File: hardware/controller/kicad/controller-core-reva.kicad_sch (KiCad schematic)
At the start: 188 parts, among them J101 12V_ISOLATED_INPUT / JST XH, J102 STM_SWD / 1x6 2.54mm, J103 ESP_UART / 1x6 2.54mm, J104 UI_LINK / WR-MM 16, J105 JP13 NTC / 2 vías, J106 JP5 FLOW ADAPTER / VCC-GND-OC, J107 JP14 DOOR / contacto seco, J108 JP16 VISUAL V1..V8 / XH-8, J109 JP22 WATER / RED-WHITE-BLACK, J110 USB-C SERVICE / USB 2.0, J111 USB BENCH POWER / OPEN, J112 24V_ACTUATOR_INPUT / JST XH, J113 JP3 VALVE / A2506, J114 POWER MONITOR / MEASURE ONLY, J115 JP8 GRINDER / 320VDC, J116 JP19 HEATER / 1900W 27R5, J117 JP24 PUMP / 230VAC, J118 JP17 MAINS / L-N, J119 JP1 PE TO BOILER, J120 JP9 PE INPUT, J121 24V INTERNAL SELECT / OPEN FO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, K701 G5RL-1A-E-TV8 DC24, Q501 SI2308A, Q701 SI2308A / relay coil, Q703 BTA24-800BWRG / heater, Q704 BTA24-800BWRG / pump, Q705 SI2308A / heater opto LED, Q706 SI2308A / pump opto LED, Q707 SI2308A / grinder opto LED, Q708 BTA24-800BWRG / grinder, U101 STM32G431RBT6, U201 ESP32-S3-WROOM-1U-N8R8, U203 USBLC6-2SC6, U301 AP63203WU-7, U302 TPS22918DBVR, U303 AP63200WU-7 / 24V to 12V, U501 DRV8876PWPR, U502 UCC27517DBVR, U601 TPS3828-33DBVR, U602 SN74LVC2G08DCTR, U603 SN74LVC2G08DCTR, U604 SN74LVC2G08DCTR, U701 MOC3083 / zero-cross, U702 MOC3083 / zero-cross, U703 MOC3083 / zero-cross

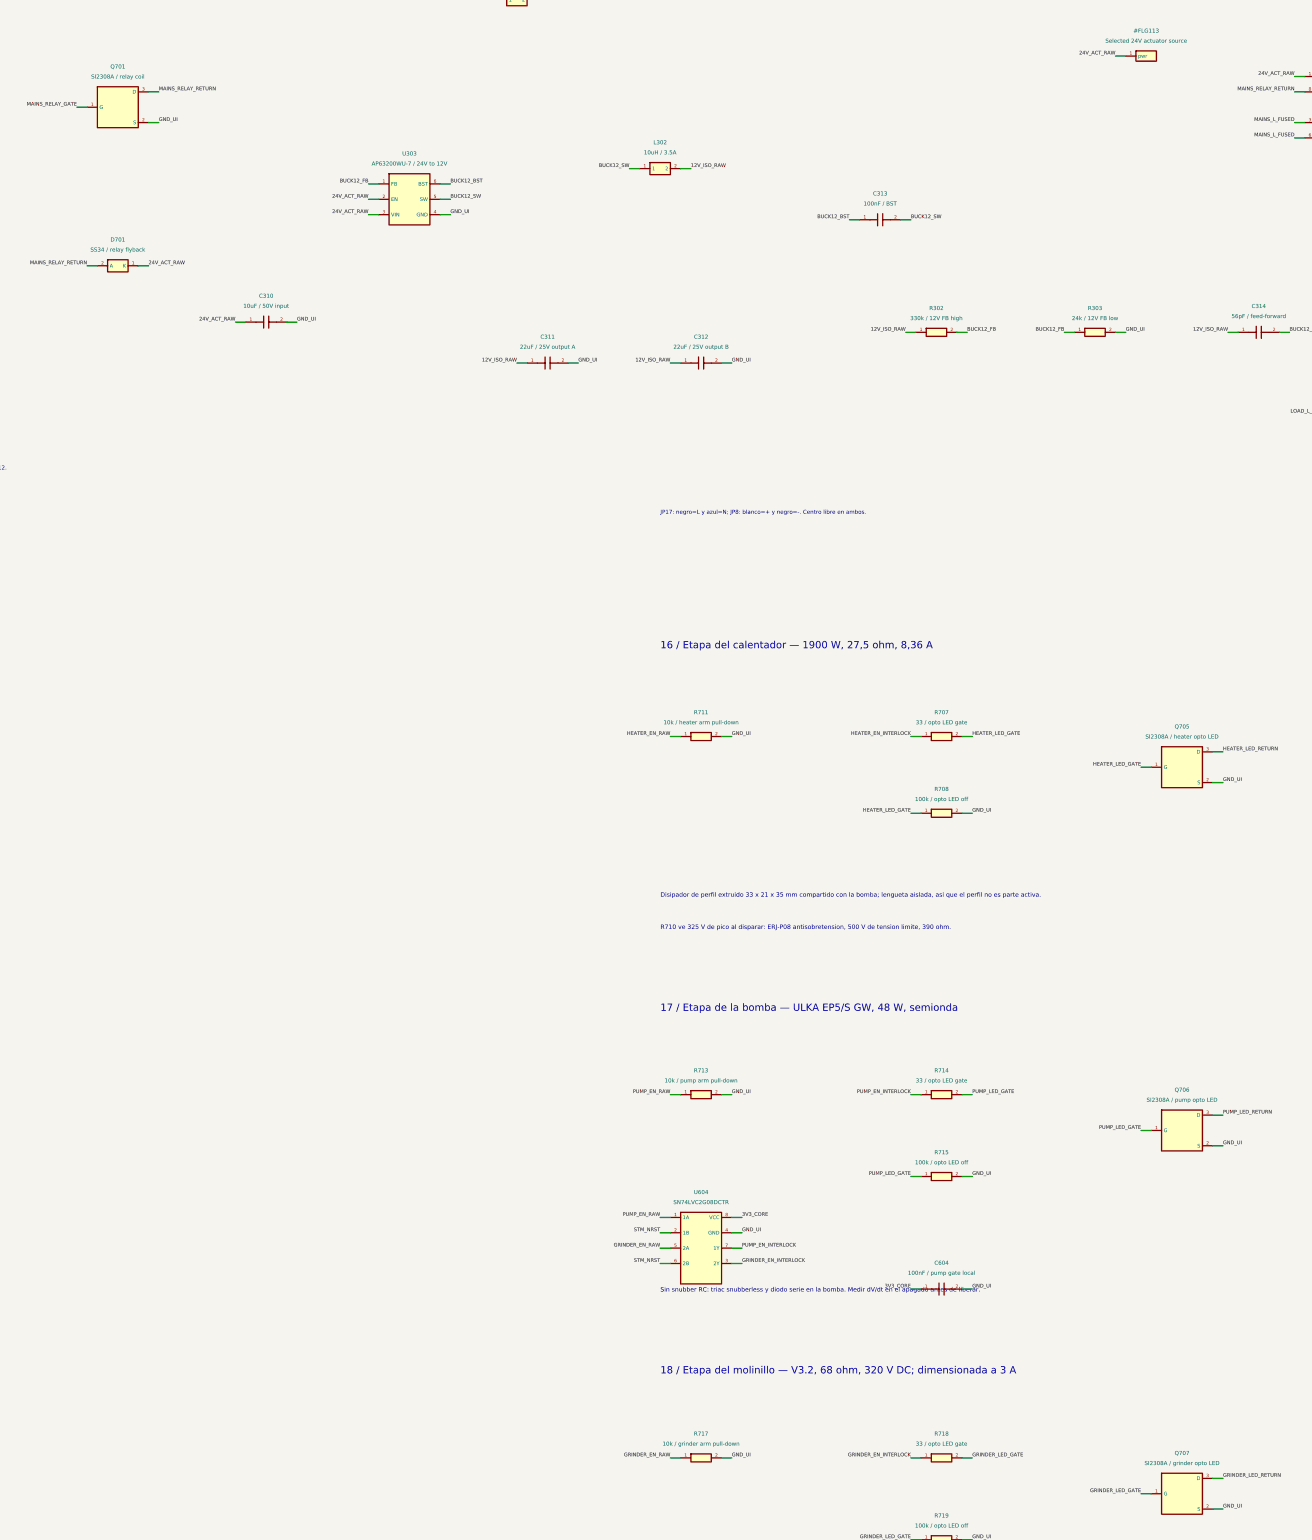
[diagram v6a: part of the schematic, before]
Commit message: Add F1 of the simulator and drive the relay and opto MOSFETs from 3.3 V
F1: sim/osc_sim/circuit.py solves both boards as a switch-level DC
network built from the netlists, with the guaranteed limits of every
active part in sim/reference/devices.json (datasheet per part). The new
'drive' rule (sim/osc_sim/drive.py) requires every order to move its load
at both ends of the rails: active, inactive, with the MCU in reset and,
when interlocked, with STM_NRST low and the pin still driven. Anything
between two guaranteed points is undefined and fails. The report gains a
worst-case margin table.

The STM32 gets osc_hal.h, a BSP and a main loop (WDI every 100 ms). The
firmware is built for the host over sim/hal/hal_sim.c, loaded with ctypes
and run on the virtual board in 1 ms steps (sim/osc_sim/board.py) with
U601 at its harshest timings and a simple plant (sim/osc_sim/plant.py,
assumed values marked). Nine scenarios in tests/sim/test_f1.py: boot at
both corners, a quiet watchdog at 0.9 s, a hung core reset within 2.5 s,
runaway orders cut by the interlock in the same step, the UCPD dead-
battery Rd, boiler/NTC, brew unit/IPROPI and flow meter edges.

Its first run found one error on the main board: Q701 (K701 coil) and
Q705-Q707 (opto LEDs) were SI2308A with their gate at 3.3 V from the
LVC2G08 gates. UMW only specifies RDS(on) from VGS = 4.5 V and VGS(th)
reaches 3 V, so at the low corner none of the mains orders was
guaranteed. They become onsemi BSS138LT1G (C82045): VGS(th) 0.5-1.5 V,
10 ohm max at VGS = 2.75 V, 50 V. Same SOT-23 pinout, so placement and
routing are untouched. Q501 keeps the SI2308A on the UCC27517's 12 V.
Worst case now: VGS 3.20 V, opto IF 9.5 mA (IFT 5 mA), coil 21.5 V
(must operate 16.8 V). Four mutation tests cover the new checks.

ERC 0 on both boards; netlist 188/614; DRC: 0 violations, 0 unconnected,
parity only MH1-MH3; board model 0 errors, 0 warnings; tests/sim 33/33;
CTest 2/2.

Co-Authored-By: Claude Opus 5.5 <noreply@anthropic.com>
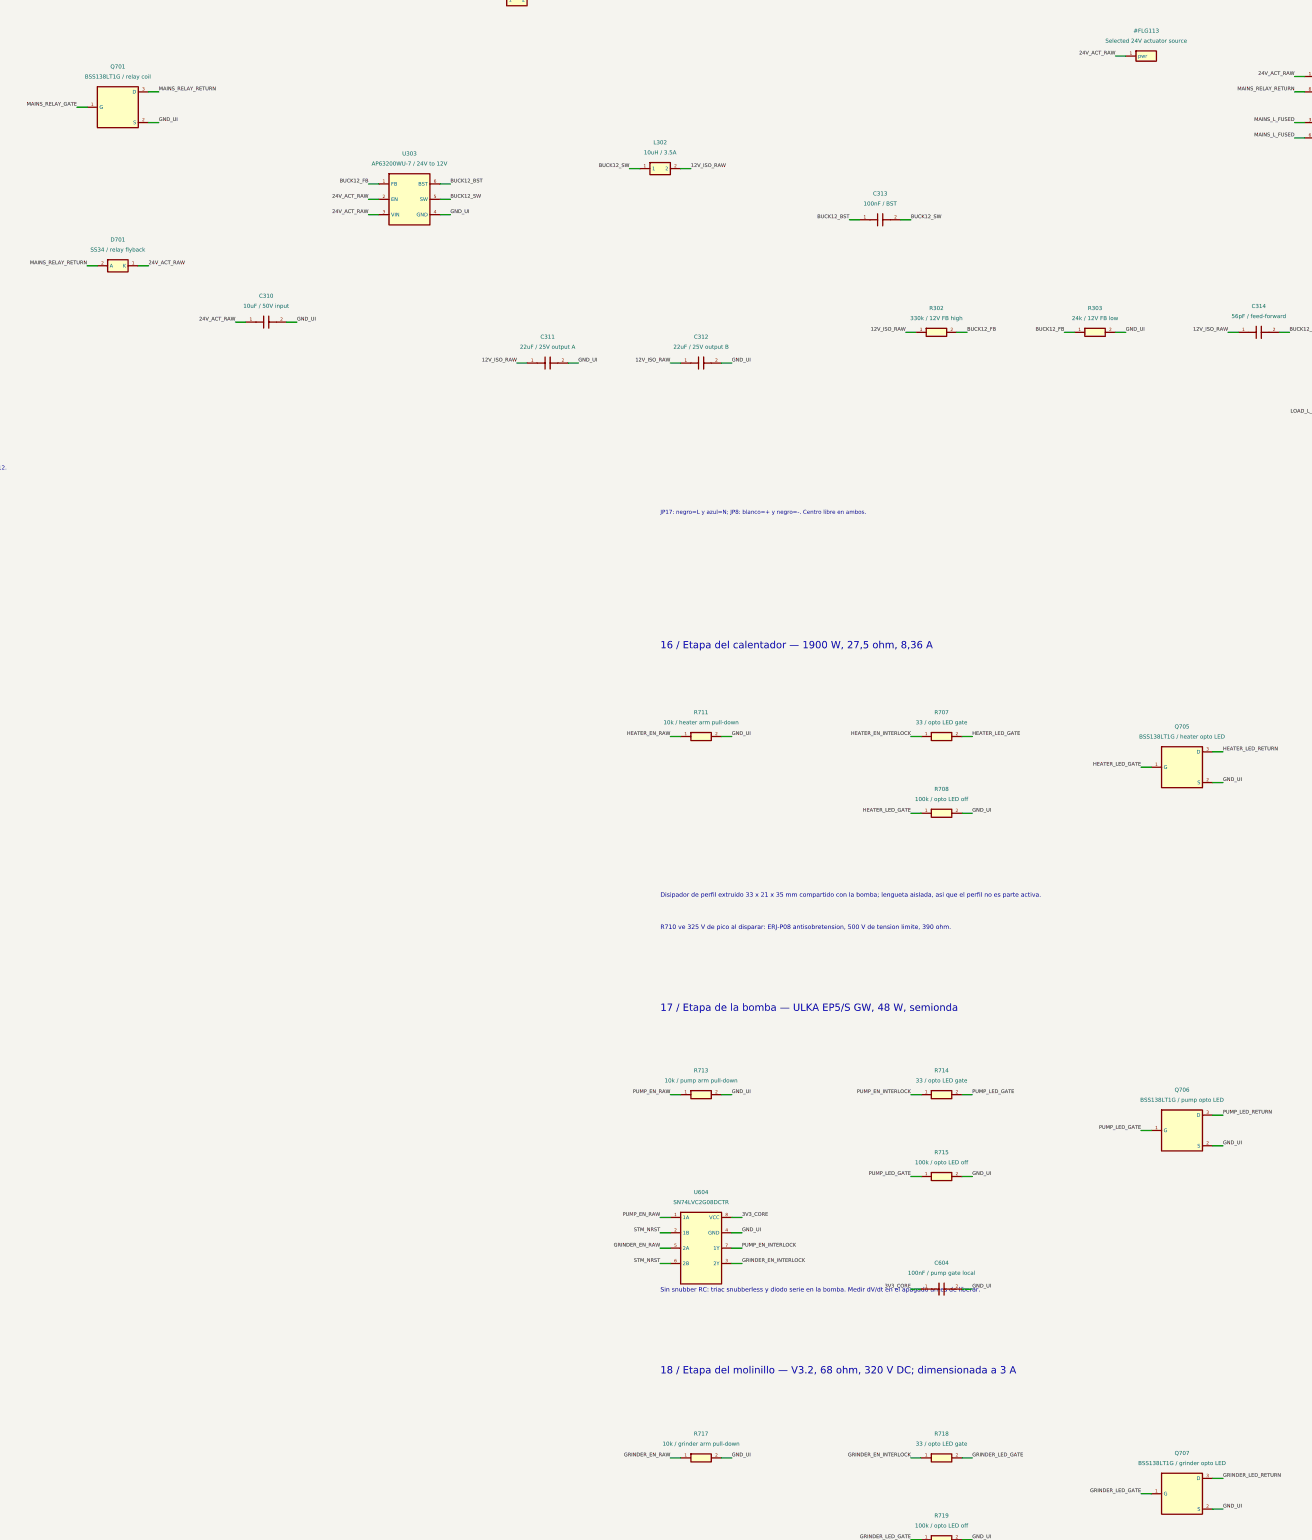
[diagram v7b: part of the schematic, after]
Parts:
- Q701: value SI2308A / relay coil -> BSS138LT1G / relay coil; lcsc C347491 -> C82045; manufacturer UMW -> onsemi; mpn SI2308A -> BSS138LT1G
- Q705: value SI2308A / heater opto LED -> BSS138LT1G / heater opto LED; lcsc C347491 -> C82045; manufacturer UMW -> onsemi; mpn SI2308A -> BSS138LT1G
- Q706: value SI2308A / pump opto LED -> BSS138LT1G / pump opto LED; lcsc C347491 -> C82045; manufacturer UMW -> onsemi; mpn SI2308A -> BSS138LT1G
- Q707: value SI2308A / grinder opto LED -> BSS138LT1G / grinder opto LED; lcsc C347491 -> C82045; manufacturer UMW -> onsemi; mpn SI2308A -> BSS138LT1G

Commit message: Square STM_NRST with a Schmitt buffer for the interlock gates
The new slow-edge rule of the simulator (sim/osc_sim/drive.py) checks that
logic inputs without hysteresis do not hang on a slow RC. It found the six
reset inputs of U602-U604 (SN74LVC2G08) on STM_NRST, which rises through
R101 (10k, with the STM32's own pull-up) into C101 (100 nF): about
530 us/V, where TI SCES198N allows 10 ns/V at 3.3 V. With an order active,
the falling edge of a watchdog reset could make a gate output oscillate
before it settles low. No Schmitt-input equivalent fits the SM-8 footprint.

U605, an SN74LVC1G17DBVR (TI, C7836) with C605 = 100 nF, takes STM_NRST
and drives STM_NRST_BUF to the six inputs (VT+ 1.92 V max, VT- 0.89 V min
at 3 V, no transition limit). U601, R101, C101, the MCU and J102 stay on
STM_NRST. On the PCB U605 sits in the pocket under R603: the reset column
is cut at y = 61 mm and drops to B.Cu to reach U605's input between its
pad rows; the output takes the column on to U602, U603 and U604. C605 is
south of the heater order with vias to both planes.

The interlock check now accepts STM_NRST through non-inverting buffers,
the circuit model knows the Schmitt buffer, and two mutation tests cover
the rule and the buffered interlock.

ERC 0 on both boards; netlist 190/621; DRC with all severities:
0 violations, 0 unconnected, parity only MH1-MH3 (1326 segments, 445 vias,
153 stitching); board model 0 errors, 0 warnings; tests/sim 35/35.
Silkscreen, 1:1 PDF and render regenerated.

Co-Authored-By: Claude Opus 5.5 <noreply@anthropic.com>
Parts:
- added C605: 100nF / reset buffer local, Capacitor_SMD:C_0603_1608Metric, symbol OpenSaeco:C
- added U605: SN74LVC1G17DBVR, Package_TO_SOT_SMD:SOT-23-5, symbol OpenSaeco:SCHMITT_BUF
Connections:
- net 3V3_CORE: now also C605.1, U605.5 (VCC)
- net GND_UI: now also C605.2, U605.3 (GND)
- net STM_NRST: now also U605.2 (A); no longer U602.2 (1B), U602.6 (2B), U603.2 (1B), U603.6 (2B), U604.2 (1B), U604.6 (2B)
- new net STM_NRST_BUF: U602.2 (1B), U602.6 (2B), U603.2 (1B), U603.6 (2B), U604.2 (1B), U604.6 (2B), U605.4 (Y)
- no-connect marks 60 -> 61
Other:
- note added: "~RESET open-drain comparte STM_NRST; U605 (Schmitt) lo cuadra para las AND U602-U604."
- note removed: "~RESET open-drain comparte STM_NRST y fuerza ambas salidas a 0 mediante U602."
